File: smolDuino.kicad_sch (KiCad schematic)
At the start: 52 parts, among them J1 Barrel_Jack_Switch, J2 USB_C_Receptacle_USB2.0, J3 2x3 SPI Header, J4 2x5 HV Outputs, J5 I^{2}C Connector, P1 CONN_01X01, P2 CONN_01X01, P3 CONN_01X01, P4 CONN_01X01, P5 Digital, P6 Power, P7 Digital, P8 Analog, Q1 AO3401A, SW1 Enable, SW2 Reset, U1 AP62250smol_A, U2 rp2040smol-c-unit, U3 74AHCT1G04, U4 Charj_smol, U5 AT24CS02-STUM, U6 SN74AHCT125N

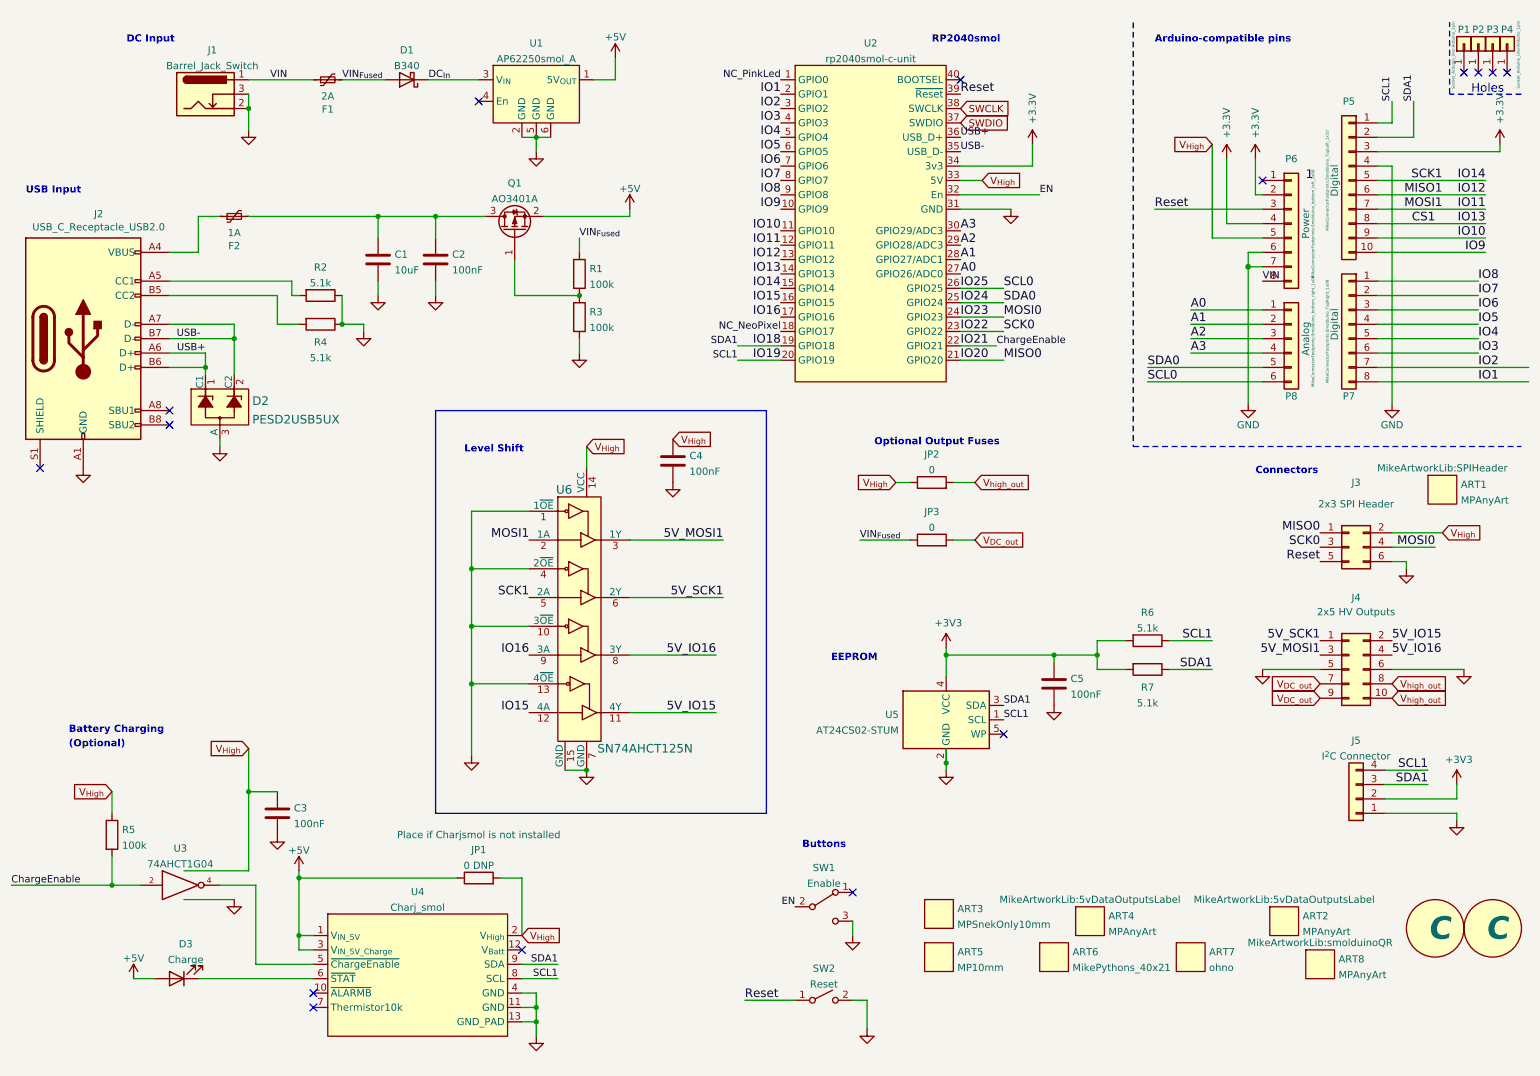
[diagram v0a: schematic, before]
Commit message: Removed Charjsmol and integrated the charge circuit directly onto the board. Other than the BGA gas gauge IC (which could be deleted without a huge loss) there's no real reason to put the charger on a smol board.
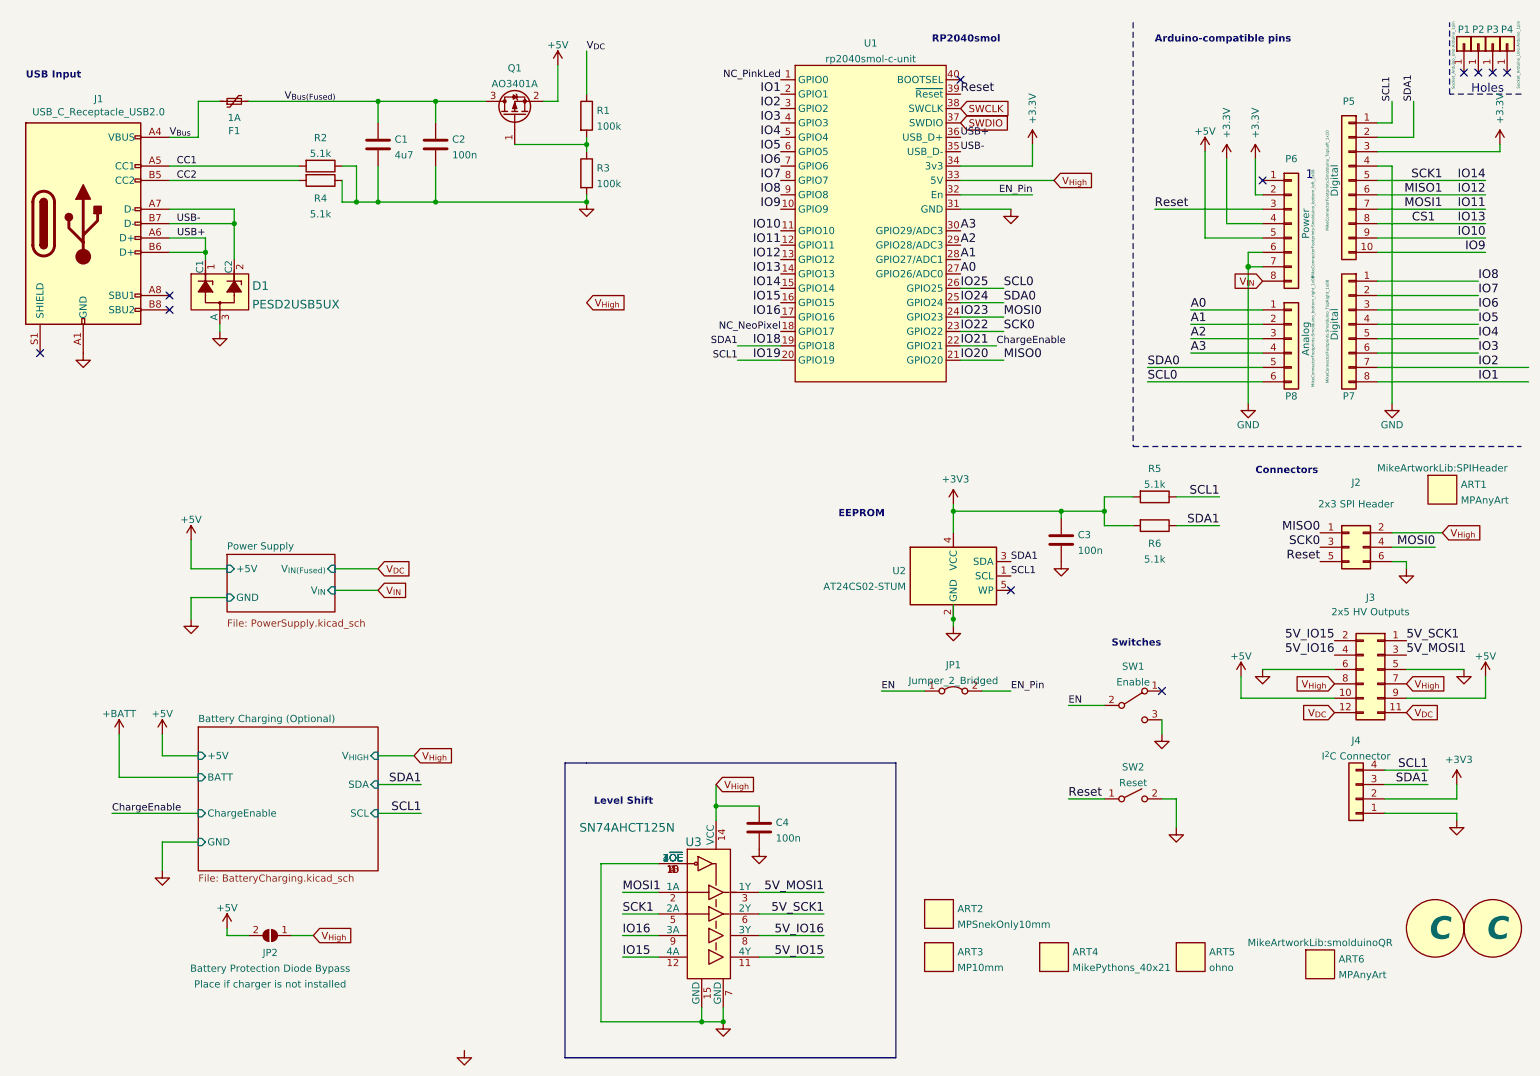
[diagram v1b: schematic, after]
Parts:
- removed ART2, ART4: MPAnyArt, MikeArtworkLib:5vDataOutputsLabel, symbol MikeArtworkLib:MPAnyArt
- removed C3: 100nF, Capacitor_SMD:C_0603_1608Metric, symbol Device:C
- removed D1: B340, Diode_SMD:D_SMC, symbol Diode:B340
- removed D3: Charge, LED_SMD:LED_0603_1608Metric, symbol Device:LED
- removed F1: 2A, Fuse:Fuse_2920_7451Metric, symbol Device:Polyfuse_Small
- removed J1: Barrel_Jack_Switch, Connector_BarrelJack:BarrelJack_GCT_DCJ200-10-A_Horizontal, symbol Connector:Barrel_Jack_Switch
- removed JP1: 0 DNP, MikeFootprintLib:R_0OHM_1206_3216Metric, symbol Device:R
- removed JP2, JP3: 0, MikeFootprintLib:R_0OHM_1206_3216Metric, symbol Device:R
- removed R5: 100k, Resistor_SMD:R_0603_1608Metric, symbol Device:R
- removed U1: AP62250smol_A, MikePCBAs:AP62250smol_A, symbol MikeLib:AP62250smol_A
- removed U3: 74AHCT1G04, Package_TO_SOT_SMD:SOT-353_SC-70-5, symbol 74xGxx:74AHCT1G04
- removed U4: Charj_smol, MikePCBAs:Charj_smol_B, symbol MikeLib:Charj_smol
- added JP1: Jumper_2_Bridged, Jumper:SolderJumper-2_P1.3mm_Bridged_Pad1.0x1.5mm, symbol Jumper:Jumper_2_Bridged
- added JP2: Battery Protection Diode Bypass, Jumper:SolderJumper-2_P1.3mm_Open_TrianglePad1.0x1.5mm, symbol Jumper:SolderJumper_2_Open
- C1: value 10uF -> 4u7
- C2, C4: value 100nF -> 100n
- C3: renamed from C5; value 100nF -> 100n
- J3: renamed from J4; footprint MikeConnectorFootprints:smolduino_2x05_header -> MikeConnectorFootprints:PinSocket_2x06_P2.54mm_Vertical; symbol Connector_Generic:Conn_02x05_Odd_Even -> Connector_Generic:Conn_02x06_Odd_Even
- P1, P2, P3, P4: now left out of the parts list
- U3: renamed from U6; symbol MikeLib:SN74AHCT125N -> MikeLib:SN74AHCT125N_OETied
- renumbered ART3 to ART2, ART5 to ART3, ART6 to ART4, ART7 to ART5, ART8 to ART6, D2 to D1, F2 to F1, J2 to J1, J3 to J2, J5 to J4, R6 to R5, R7 to R6, U2 to U1, U5 to U2
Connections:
- net +5V: now also J3.10 (Pin_10), J3.9 (Pin_9), P6.5 (Pin_5), JP2.2 (B)
- net EN: now also JP1.1 (A); no longer U1.32 (En)
- net CC2: now reaches J1.B5 (CC2), R4.2
- net V_{Bus}: now reaches F1.1, J1.A4 (VBUS), J1.A9 (VBUS), J1.B4 (VBUS), J1.B9 (VBUS)
- net CC1: now reaches J1.A5 (CC1), R2.2
- net V_{Bus}_{(Fused)}: now reaches C1.2, C2.1, F1.2, Q1.3 (D)
- net VCC renamed V_{High}
- net V_{High}: now also J3.7 (Pin_7), J3.8 (Pin_8), JP2.1 (A); no longer P6.5 (Pin_5)
- net VIN renamed V_{IN}
- net VIN_{Fused} renamed V_{DC}
- net V_{DC}: now also J3.11 (Pin_11), J3.12 (Pin_12)
- removed net V_{DC_out}: J3.7 (Pin_7), J3.9 (Pin_9)
- removed net V_{high_out}: J3.10 (Pin_10), J3.8 (Pin_8)
- new net EN_Pin: JP1.2 (B), U1.32 (En)
- no-connect marks 15 -> 11
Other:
- added sheet Battery Charging (Optional) (BatteryCharging.kicad_sch)
- added sheet Power Supply (PowerSupply.kicad_sch)
- note added: "Switches"
- note removed: "(Optional)"
- note removed: "Battery Charging"
- note removed: "Buttons"
- note removed: "DC Input"
- note removed: "Optional Output Fuses"
- moved on the sheet: C1, C2, C3, C4, D1, F1, J1, Q1, R1, R2, R3, R4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
